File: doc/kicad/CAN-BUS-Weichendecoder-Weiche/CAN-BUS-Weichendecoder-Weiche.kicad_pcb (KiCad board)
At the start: 2 copper layers, 151.1 x 88.9 mm, 39 parts, among them J1 250-1404, J1001 I²C, J1002 Conn_01x16_Male, J2 250-1404, J22 J22, J23 J22, J3 250-1404, J31 12V DC, J4 250-1404, J41 2604-1102, J5 250-1404, U1 Arduino_Nano, U10 TSR_1-2450, U1001 6N136, U2 ULN2803A, U3 ULN2803A

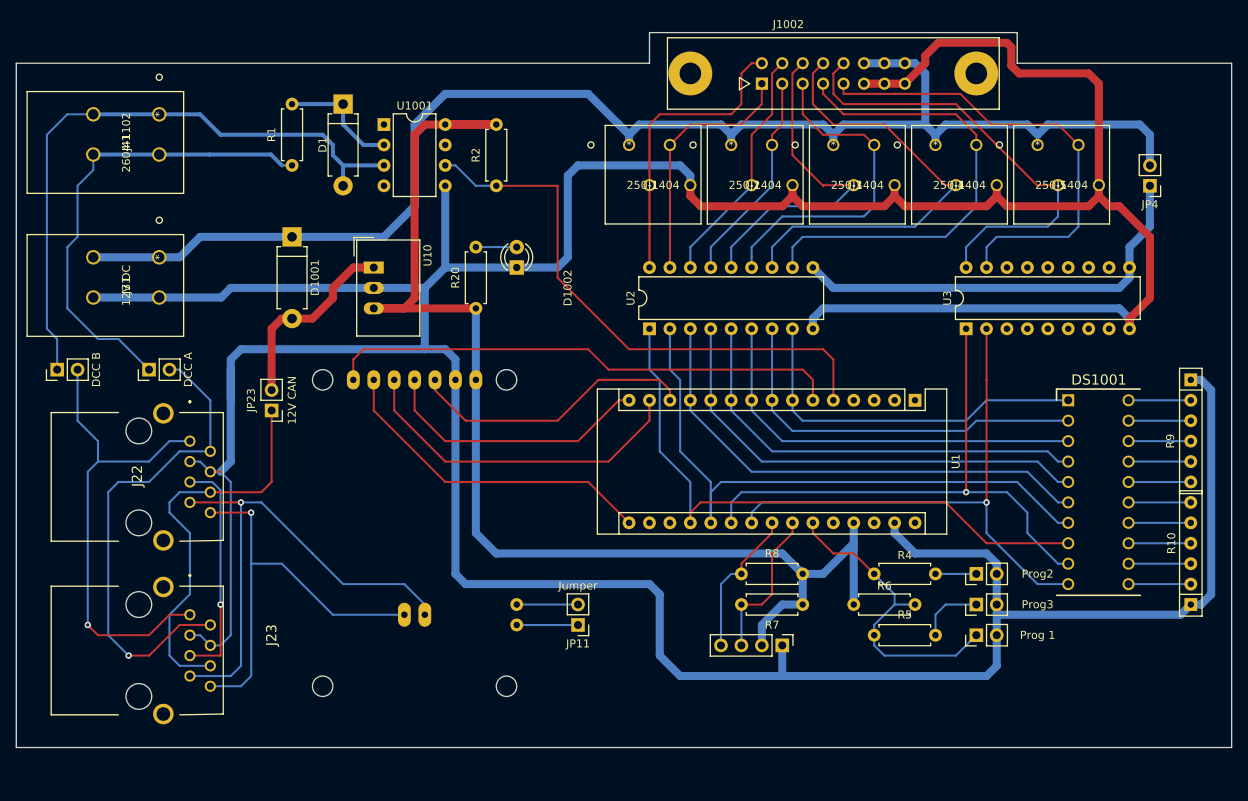
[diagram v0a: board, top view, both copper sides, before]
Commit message: Buchen und Stecker vertauscht und Anordnung kompakter
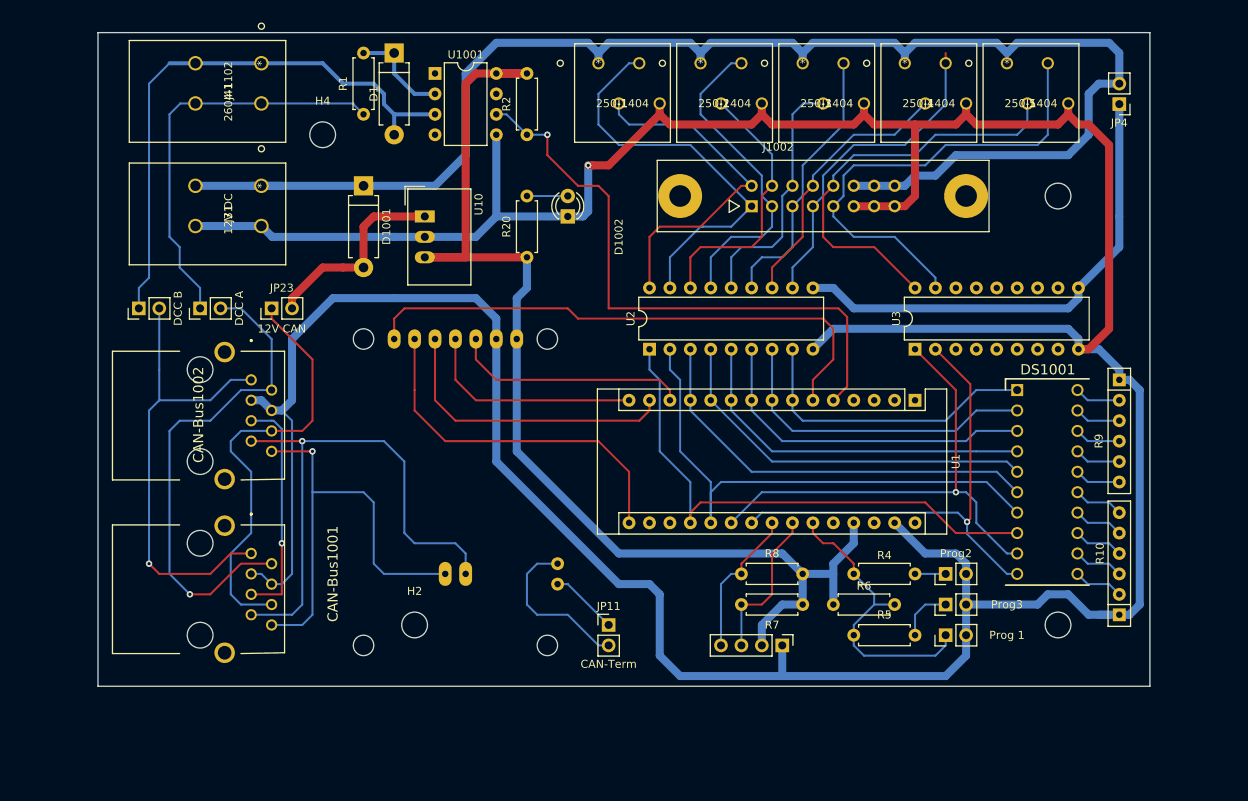
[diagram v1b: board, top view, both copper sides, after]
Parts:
- added H1: MountingHole, Mounting_Holes:MountingHole_3.2mm_M3, F.Cu at (153.7, 95.2)
- added H2: MountingHole, Mounting_Holes:MountingHole_3.2mm_M3, F.Cu at (73.7, 95.2)
- added H3: MountingHole, Mounting_Holes:MountingHole_3.2mm_M3, F.Cu at (153.7, 41.9)
- added H4: MountingHole, Mounting_Holes:MountingHole_3.2mm_M3, F.Cu at (62.2, 34.3)
- JP11: value Jumper -> CAN-Term
- moved J31 15.5 mm to (54.6, 40.6)
- moved J1002 15.3 mm to (115.6, 43.2)
- moved J41 14.2 mm to (54.6, 25.4)
- moved JP23 12.7 mm to (55.9, 55.9), turned to 90 degrees
- moved JP41 12.7 mm to (39.4, 55.9)
- moved D1001 10.9 mm to (67.3, 40.6)
- moved R1 10.9 mm to (67.3, 24.1)
- moved J1 10.9 mm to (96.5, 25.4)
- moved J2 10.9 mm to (109.2, 25.4)
- moved J3 10.9 mm to (121.9, 25.4)
- moved J4 10.9 mm to (134.6, 25.4)
- moved J5 10.9 mm to (147.3, 25.4)
- moved JP4 10.9 mm to (161.3, 30.5)
- moved CAN-Bus1001 10.8 mm to (53.3, 86.4)
- moved CAN-Bus1002 10.8 mm to (53.3, 64.8)
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- renumbered J23 to CAN-Bus1001, J22 to CAN-Bus1002
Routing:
- net GND: track 552.4 -> 478.8 mm, vias 0 -> 1
- net Net-(J1002-Pad8): track 56.1 -> 33.7 mm
- net Net-(J1-Pad3): track 31.3 -> 50.6 mm
- net Net-(J1002-Pad7): track 58.8 -> 40.8 mm
- net Net-(J1002-Pad3): track 26.5 -> 39.9 mm
- net Net-(JP11-Pad2): track 7.62 -> 20.4 mm
- net +5V: track 156.9 -> 145.4 mm
- net +12V: track 177.8 -> 189.2 mm
- net Net-(J1002-Pad6): track 42.2 -> 31.3 mm
- net Net-(DS1001-Pad5): track 58.3 -> 48.1 mm
- net Net-(DS1001-Pad6): track 61.9 -> 52.5 mm
- net Net-(DS1001-Pad4): track 55.6 -> 46.2 mm
- net Net-(DS1001-Pad8): track 77.1 -> 67.7 mm
- net Net-(DS1001-Pad7): track 77.1 -> 67.7 mm
- net Net-(DS1001-Pad9): track 70.5 -> 61.7 mm
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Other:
- board size 151.1 x 88.9 mm -> 130.8 x 81.3 mm

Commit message: Anordnung der Bauteile kompakter, 2 statt 3 prog-Pins, nur eine Verbindung zur Weiche
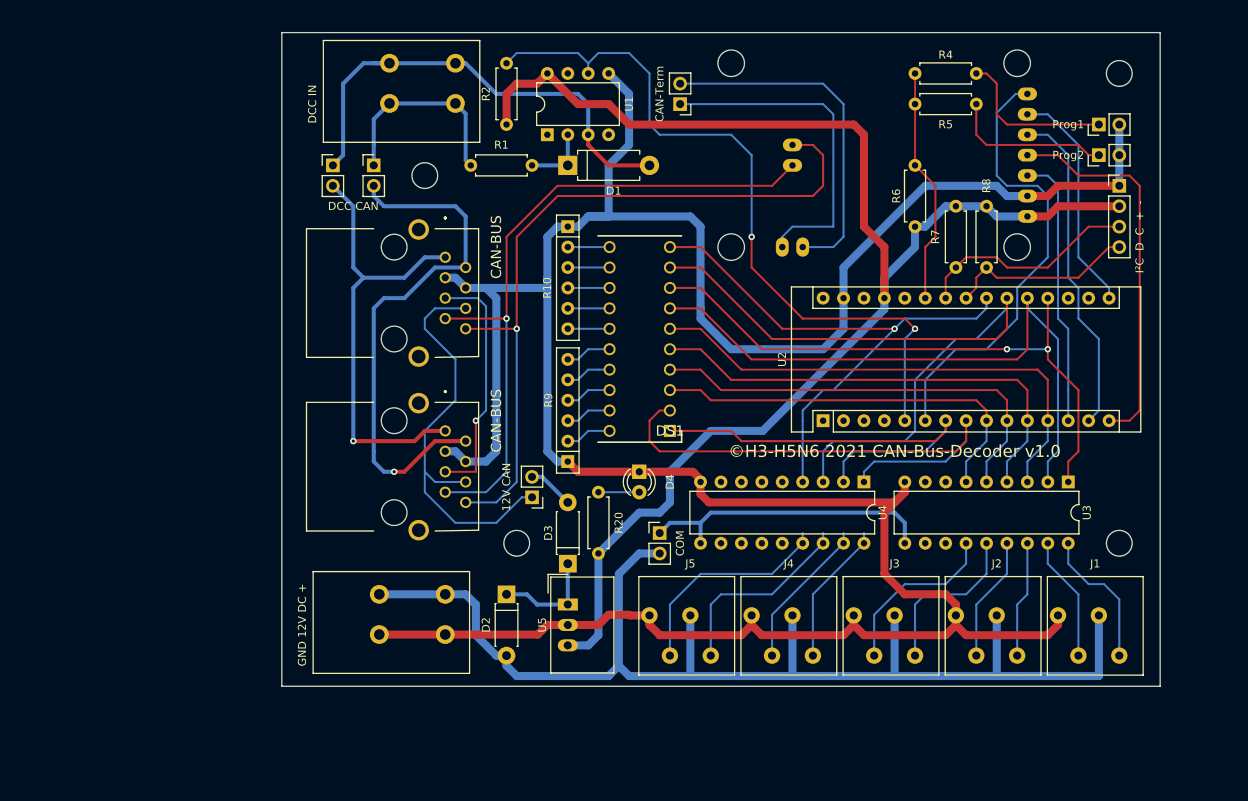
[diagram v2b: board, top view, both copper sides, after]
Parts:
- removed D1001: DIODE, Diodes_THT:D_DO-15_P10.16mm_Horizontal
- removed DS1001: DC-10SGWA, Kingbright-LED:DIPS750W80P254L2540H825Q20N
- removed J1002: Conn_01x16_Male, Connectors:he10-16d
- removed J31: 12V DC, CONN_2604-1102_4_WAG
- removed J41: 2604-1102, CONN_2604-1102_4_WAG
- removed the JP1 at (139.7, 96.5)
- removed Shield1001: CAN-BUS_MODULE_TJA1050, CAN-BUS-MODULE:MCP2515_CAN_MODULE_BY0-10
- removed the U1 at (135.9, 67.3)
- added D2: 1N4001, Diodes_THT:D_DO-41_SOD81_P7.62mm_Horizontal, F.Cu at (85.1, 91.4)
- added D3: 1N4001, Diodes_THT:D_DO-41_SOD81_P7.62mm_Horizontal, F.Cu at (92.7, 87.6)
- added DS1: DC-10SGWA, Kingbright-LED:DIPS750W80P254L2540H825Q20N, F.Cu at (105.4, 71.1)
- added J6: GND 12V DC +, CONN_2604-1102_4_WAG, F.Cu at (77.5, 91.4)
- added J7: DCC IN, CONN_2604-1102_4_WAG, F.Cu at (78.7, 25.4)
- added Shield1: CAN-BUS-MODULE, CAN-BUS-MODULE:MCP2515_CAN_MODULE, B.Cu at (152.4, 50.8)
- added U2: Arduino_Nano, Modules:Arduino_Nano, F.Cu at (124.5, 69.8)
- J1, J2, J3, J4, J5: footprint Wago:250-1404 -> Wago:CONN_250-1404_WAG
- J22: renamed from CAN-Bus1001; value J22 -> CAN-BUS
- J23: renamed from CAN-Bus1002; value J22 -> CAN-BUS
- J8: renamed from J1001; value I²C -> I²C D C + -
- JP2: renamed from JP42; value DCC A -> DCC CAN
- JP5: renamed from JP2; value Prog2 -> Prog1
- JP6: renamed from JP3; value Prog3 -> Prog2
- JP7: renamed from JP4; value Jumper -> COM
- moved J1 98.1 mm to (161.3, 99.1), turned to 180 degrees
- moved R10 83.9 mm to (92.7, 45.7), turned to 270 degrees
- moved J2 83.5 mm to (148.6, 99.1), turned to 180 degrees
- moved J5 82.4 mm to (110.5, 99.1), turned to 180 degrees
- moved JP7 78.2 mm to (104.1, 83.8), turned to 0 degrees
- moved J3 75.0 mm to (135.9, 99.1), turned to 180 degrees
- moved J4 74.5 mm to (123.2, 99.1), turned to 180 degrees
- moved J8 70.9 mm to (161.3, 40.6), turned to 0 degrees
- moved R9 69.3 mm to (92.7, 74.9), turned to 90 degrees
- moved R5 66.5 mm to (135.9, 30.5)
- moved JP3 65.4 mm to (106.7, 30.5), turned to 180 degrees
- moved R4 62.7 mm to (135.9, 26.7)
- moved JP5 59.0 mm to (158.8, 33.0)
- moved JP6 59.0 mm to (158.8, 36.8)
- moved U3 54.6 mm to (154.9, 77.5), turned to 270 degrees
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- renumbered D1002 to D4, JP41 to JP1, JP11 to JP3, JP23 to JP4, U1001 to U1, U2 to U3, U3 to U4, U10 to U5
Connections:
- J1 pad 1: +12V -> Net-(J1-Pad1)
- J1 pad 2: Net-(J1-Pad2) -> +12V
- J2 pad 1: +12V -> Net-(J2-Pad1)
- J2 pad 2: Net-(J1002-Pad4) -> +12V
- J3 pad 1: +12V -> Net-(J3-Pad1)
- J3 pad 2: Net-(J1002-Pad6) -> +12V
- J4 pad 1: +12V -> Net-(J4-Pad1)
- J4 pad 2: Net-(J1002-Pad8) -> +12V
- J4 pad 3: Net-(J1002-Pad7) -> Net-(J4-Pad3)
- J5 pad 1: +12V -> Net-(J5-Pad1)
- J5 pad 2: Net-(J1002-Pad10) -> +12V
- J5 pad 3: Net-(J1002-Pad9) -> Net-(J5-Pad3)
- JP4 pad 2: Net-(D1001-Pad2) -> Net-(D3-Pad2)
- U3 pad 11: Net-(J1002-Pad7) -> (no net)
- U3 pad 12: Net-(J1002-Pad8) -> (no net)
- U3 pad 14: Net-(J1002-Pad6) -> Net-(J3-Pad1)
- U3 pad 16: Net-(J1002-Pad4) -> Net-(J2-Pad1)
- U3 pad 18: Net-(J1-Pad2) -> Net-(J1-Pad1)
- U3 pad 7: Net-(DS1001-Pad2) -> (no net)
- U3 pad 8: Net-(DS1001-Pad1) -> (no net)
- U4 pad 15: (no net) -> Net-(J5-Pad3)
- U4 pad 16: (no net) -> Net-(J5-Pad1)
- U4 pad 17: Net-(J1002-Pad9) -> Net-(J4-Pad3)
- U4 pad 18: Net-(J1002-Pad10) -> Net-(J4-Pad1)
- U4 pad 3: (no net) -> Net-(DS1-Pad9)
- U4 pad 4: (no net) -> Net-(DS1-Pad10)
- U5 pad 1: Net-(D1001-Pad2) -> Net-(D2-Pad1)
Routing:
- net GND: track 478.8 -> 369.6 mm, vias 1 -> 0
- net Net-(DS1-Pad9): track 0.00 -> 89.0 mm
- net Net-(DS1-Pad10): track 0.00 -> 70.4 mm, vias 0 -> 1
- net Net-(Shield1001-Pad7): track 68.7 -> 0.00 mm
- net Net-(J1002-Pad9): track 59.1 -> 0.00 mm
- net Net-(Shield1-Pad7): track 0.00 -> 56.5 mm
- net Net-(J1002-Pad10): track 51.6 -> 0.00 mm
- net Net-(Shield1-Pad4): track 0.00 -> 47.8 mm
- net Net-(Shield1001-Pad6): track 45.1 -> 0.00 mm
- net Net-(J1-Pad2): track 43.2 -> 0.00 mm
- net Net-(Shield1-Pad5): track 0.00 -> 41.3 mm
- net Net-(J1002-Pad7): track 40.8 -> 0.00 mm
- net Net-(DS1001-Pad2): track 40.2 -> 0.00 mm
- net Net-(DS1001-Pad1): track 37.7 -> 0.00 mm
- net Net-(Shield1001-Pad5): track 37.1 -> 0.00 mm
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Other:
- board size 130.8 x 81.3 mm -> 109.2 x 81.3 mm
- board text added: "©H3-H5N6 2021 CAN-Bus-Decoder v1.0"

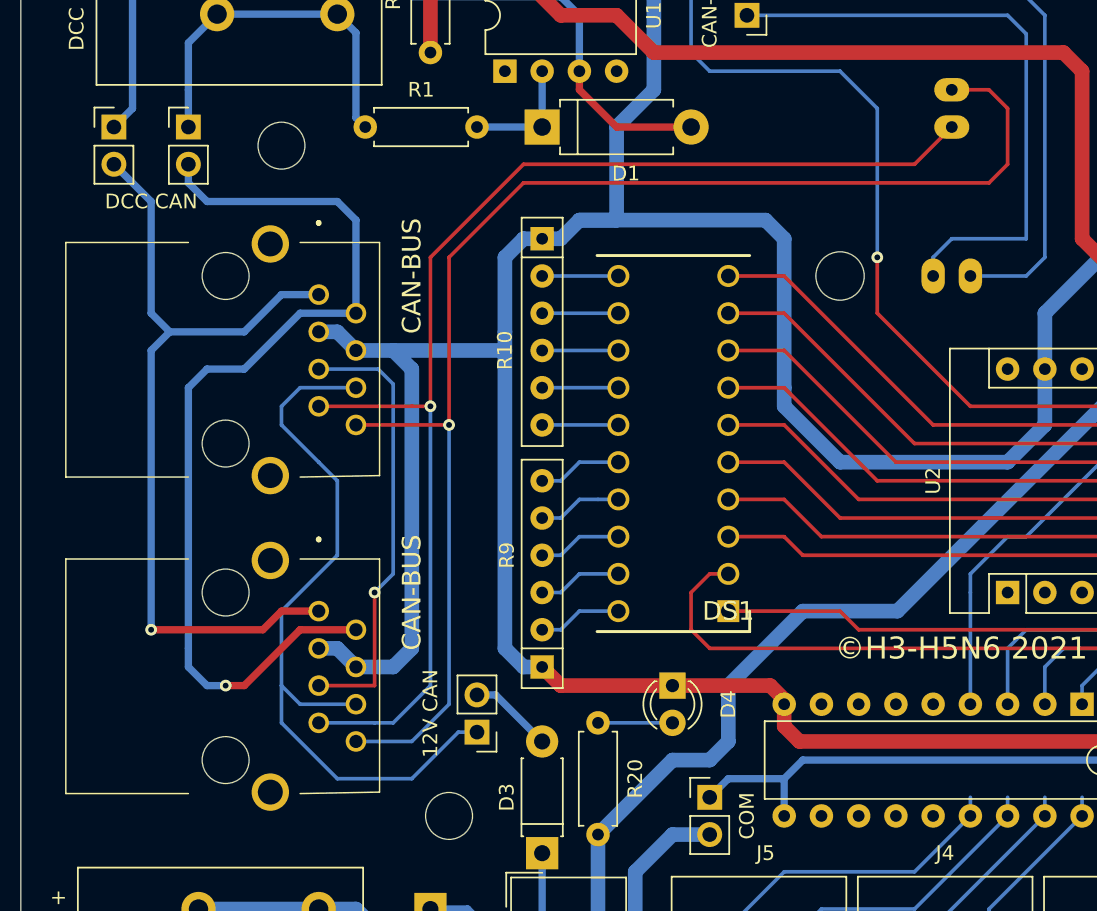
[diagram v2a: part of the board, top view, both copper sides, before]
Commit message: CAN-Bus-Belegun geändert
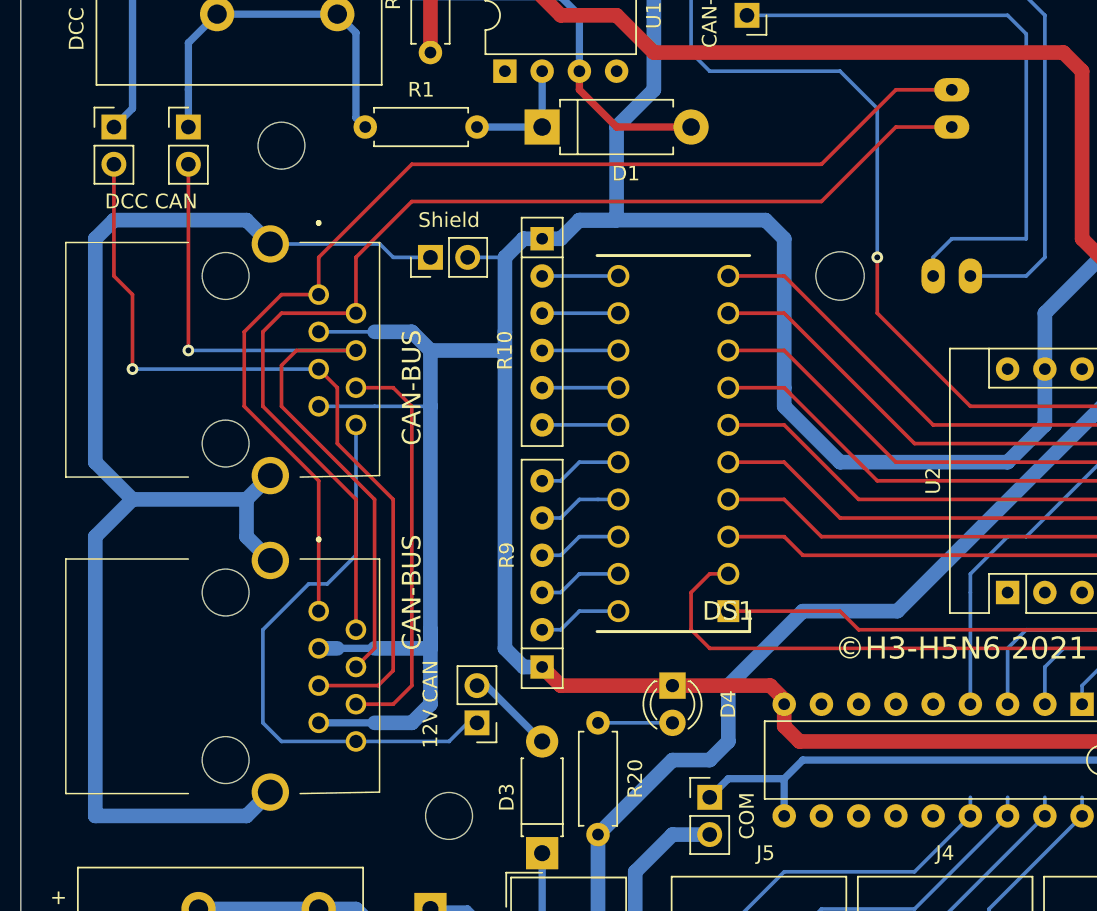
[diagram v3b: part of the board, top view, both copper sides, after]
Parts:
- added JP8: Shield, Pin_Headers:Pin_Header_Straight_1x02_Pitch2.54mm, F.Cu at (85.1, 47.0)
- moved JP4 0.64 mm to (88.3, 78.7)
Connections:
- J22 pad 4: GND -> Net-(J22-Pad4)
- J22 pad 7: Net-(J22-Pad7) -> GND
- J22 pad MH3: (no net) -> Net-(J22-PadMH3)
- J22 pad MH4: (no net) -> Net-(J22-PadMH3)
- J23 pad 4: GND -> Net-(J22-Pad4)
- J23 pad 7: Net-(J22-Pad7) -> GND
- J23 pad MH3: (no net) -> Net-(J22-PadMH3)
- J23 pad MH4: (no net) -> Net-(J22-PadMH3)
- JP1 pad 2: Net-(J22-Pad1) -> Net-(J22-Pad5)
- JP2 pad 2: Net-(J22-Pad2) -> Net-(J22-Pad4)
- JP4 pad 1: Net-(J22-Pad6) -> Net-(J22-Pad8)
- Shield1 pad H: Net-(J22-Pad8) -> Net-(J22-Pad1)
- Shield1 pad L: Net-(J22-Pad7) -> Net-(J22-Pad2)
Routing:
- net Net-(J22-PadMH3): track 0.00 -> 93.4 mm
- net Net-(J22-Pad7): track 84.7 -> 0.00 mm, vias 1 -> 0
- net Net-(J22-Pad8): track 93.1 -> 39.4 mm, vias 1 -> 0
- net Net-(J22-Pad4): track 0.00 -> 53.4 mm, vias 0 -> 1
- net Net-(J22-Pad5): track 30.4 -> 55.4 mm
- net Net-(J22-Pad6): track 52.2 -> 27.7 mm
- net GND: track 369.6 -> 392.6 mm
- net Net-(J22-Pad1): track 57.0 -> 77.7 mm, vias 1 -> 0
- net Net-(J22-Pad2): track 66.2 -> 78.0 mm, vias 1 -> 0
